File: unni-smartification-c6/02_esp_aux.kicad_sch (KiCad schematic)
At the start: 61 parts, among them J11 Conn_01x01, J12 Conn_01x01, J13 Conn_01x01, J14 Conn_01x01, J15 Conn_01x01, J17 Conn_01x01, J18 Conn_01x01, J19 Conn_01x01, J2 Li-Ion 1S JST-PH, J23 Conn_01x01, J24 Conn_01x01, J25 Conn_01x01, J26 Conn_01x01, J27 Conn_01x01, Q1 AO3401A, Q10 AO3400A touch emulator, SW1 RESET, SW2 BOOT, U1 MCP73831T-2ACI/OT, U10 ESP32-C6-MINI-1, U2 TPS63031DSK

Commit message: Clean up power nets and routing rules
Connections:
- net CONN_USB_N renamed USB_RAW_N
- net CONN_USB_P renamed USB_RAW_P
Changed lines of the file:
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@@
 	)
 	(junction
-		(at 43.18 132.715)
+		(at 43.18 132.08)
 		(diameter 0)
 		(color 0 0 0 0)
@@
 	(wire
 		(pts
-			(xy 43.18 132.715) (xy 43.18 139.7)
+			(xy 43.18 132.08) (xy 43.18 139.7)
 		)
 		(stroke
@@
 	(wire
 		(pts
-			(xy 43.18 129.54) (xy 43.18 132.715)
+			(xy 43.18 129.54) (xy 43.18 132.08)
 		)
 		(stroke
@@
 		)
 	)
-	(global_label "CONN_GND"
+	(global_label "GND"
 		(shape input)
 		(at 82.55 226.06 180)
@@
 		)
 	)
-	(global_label "CONN_VBUS"
+	(global_label "VBUS"
 		(shape input)
 		(at 77.47 243.84 270)
@@
 		)
 	)
-	(global_label "CONN_USB_P"
+	(global_label "USB_RAW_P"
 		(shape bidirectional)
 		(at 365.76 60.96 0)
@@
 		)
 	)
-	(global_label "CONN_GND"
+	(global_label "GND"
 		(shape input)
 		(at 195.58 238.76 180)
@@
 		)
 	)
-	(global_label "CONN_+BATT"
+	(global_label "+BATT"
 		(shape input)
 		(at 87.63 243.84 270)
@@
 		)
 	)
-	(global_label "CONN_VBUS"
+	(global_label "VBUS"
 		(shape input)
 		(at 43.18 217.17 180)
@@
 		)
 	)
-	(global_label "CONN_GND"
+	(global_label "GND"
 		(shape input)
 		(at 195.58 210.82 180)
@@
 		)
 	)
-	(global_label "CONN_GND"
+	(global_label "GND"
 		(shape input)
 		(at 43.18 201.93 180)
@@
 		)
 	)
-	(global_label "CONN_USB_N"
+	(global_label "USB_RAW_N"
 		(shape bidirectional)
 		(at 43.18 205.74 180)
@@
 		)
 	)
-	(global_label "CONN_USB_P"
+	(global_label "USB_RAW_P"
 		(shape bidirectional)
 		(at 43.18 209.55 180)
@@
 		)
 	)
-	(global_label "CONN_+BATT"
+	(global_label "+BATT"
 		(shape input)
 		(at 43.18 220.98 180)
@@
 		)
 	)
-	(global_label "CONN_GND"
+	(global_label "GND"
 		(shape input)
 		(at 284.48 177.8 180)
@@
 		)
 	)
-	(global_label "CONN_USB_N"
+	(global_label "USB_RAW_N"
 		(shape bidirectional)
 		(at 386.08 58.42 0)
@@
 		(unit 1)
 		(body_style 1)
-		(exclude_from_sim no)
+		(exclude_from_sim yes)
 		(in_bom yes)
 		(on_board yes)
@@
 		(unit 1)
 		(body_style 1)
-		(exclude_from_sim no)
+		(exclude_from_sim yes)
 		(in_bom yes)
 		(on_board yes)
@@
 		(unit 1)
 		(body_style 1)
-		(exclude_from_sim no)
+		(exclude_from_sim yes)
 		(in_bom yes)
 		(on_board yes)
@@
 		(unit 1)
 		(body_style 1)
-		(exclude_from_sim no)
+		(exclude_from_sim yes)
 		(in_bom yes)
 		(on_board yes)
@@
 		(unit 1)
 		(body_style 1)
-		(exclude_from_sim no)
+		(exclude_from_sim yes)
 		(in_bom yes)
 		(on_board yes)
@@
 		(unit 1)
 		(body_style 1)
-		(exclude_from_sim no)
+		(exclude_from_sim yes)
 		(in_bom yes)
 		(on_board yes)
@@
 		(unit 1)
 		(body_style 1)
-		(exclude_from_sim no)
+		(exclude_from_sim yes)
 		(in_bom yes)
 		(on_board yes)
@@
 		(unit 1)
 		(body_style 1)
-		(exclude_from_sim no)
+		(exclude_from_sim yes)
 		(in_bom yes)
 		(on_board yes)
@@
 		(unit 1)
 		(body_style 1)
-		(exclude_from_sim no)
+		(exclude_from_sim yes)
 		(in_bom yes)
 		(on_board yes)
@@
 		(unit 1)
 		(body_style 1)
-		(exclude_from_sim no)
+		(exclude_from_sim yes)
 		(in_bom yes)
 		(on_board yes)
@@
 		(unit 1)
 		(body_style 1)
-		(exclude_from_sim no)
+		(exclude_from_sim yes)
 		(in_bom yes)
 		(on_board yes)
@@
 		(unit 1)
 		(body_style 1)
-		(exclude_from_sim no)
+		(exclude_from_sim yes)
 		(in_bom yes)
 		(on_board yes)
@@
 	(symbol
 		(lib_id "power:PWR_FLAG")
-		(at 43.18 132.715 270)
+		(at 43.18 132.08 270)
 		(unit 1)
 		(body_style 1)
@@
 		(fields_autoplaced yes)
 		(property "Reference" "#FLG05"
-			(at 45.085 132.715 0)
+			(at 45.085 132.08 0)
 			(hide yes)
 			(show_name no)
@@
 		)
 		(property "Footprint" ""
-			(at 43.18 132.715 0)
+			(at 43.18 132.08 0)
 			(hide yes)
 			(show_name no)
@@
 		)
 		(property "Datasheet" ""
-			(at 43.18 132.715 0)
+			(at 43.18 132.08 0)
 			(hide yes)
 			(show_name no)
@@
 		)
 		(property "Description" "Special symbol for telling ERC where power comes from"
-			(at 43.18 132.715 0)
+			(at 43.18 132.08 0)
 			(hide yes)
 			(show_name no)
@@
 		(unit 1)
 		(body_style 1)
-		(exclude_from_sim no)
+		(exclude_from_sim yes)
 		(in_bom yes)
 		(on_board yes)
@@
 		(unit 1)
 		(body_style 1)
-		(exclude_from_sim no)
+		(exclude_from_sim yes)
 		(in_bom yes)
 		(on_board yes)

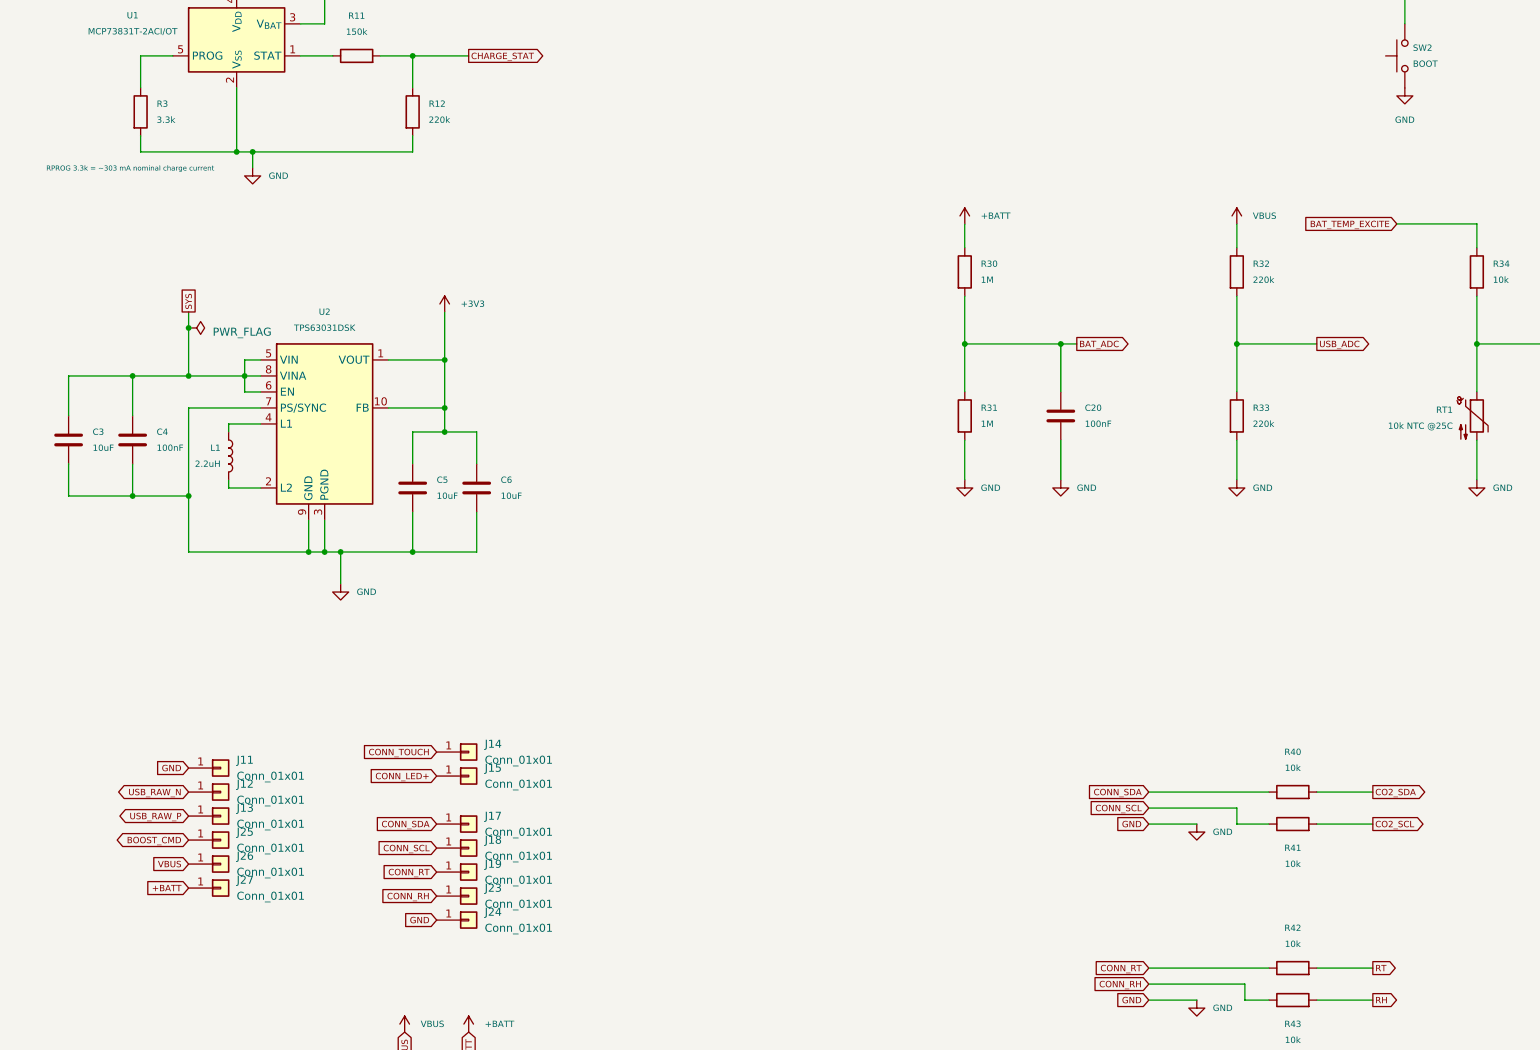
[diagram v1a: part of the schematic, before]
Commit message: new tvs diode, final fiddlings
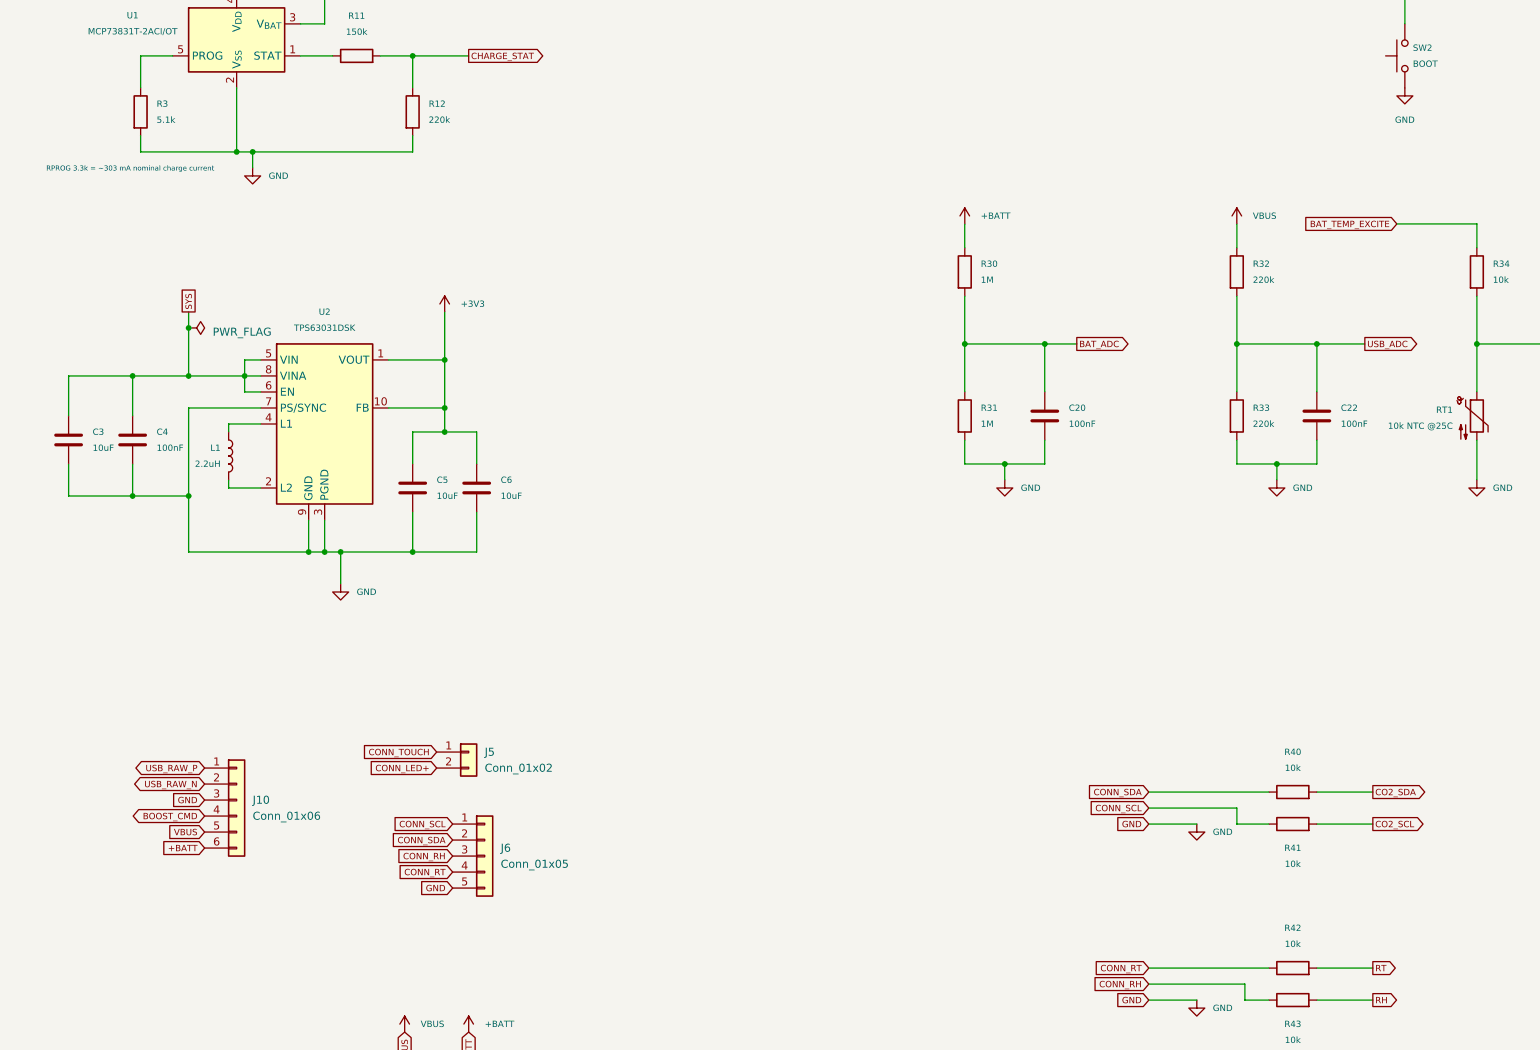
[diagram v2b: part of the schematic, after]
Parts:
- removed J11, J24: Conn_01x01, Connector_Wire:SolderWire-0.5sqmm_1x01_D0.9mm_OD2.1mm, symbol Connector_Generic:Conn_01x01
- removed J12, J13, J14, J15, J17, J18, J19, J23, J25, J26, J27: Conn_01x01, Connector_Wire:SolderWire-0.1sqmm_1x01_D0.4mm_OD1mm, symbol Connector_Generic:Conn_01x01
- added C22: 100nF, Capacitor_SMD:C_0603_1608Metric_Pad1.08x0.95mm_HandSolder, symbol Device:C
- added J10: Conn_01x06, Connector_JST:JST_PH_B6B-PH-K_1x06_P2.00mm_Vertical, symbol Connector_Generic:Conn_01x06
- added J5: Conn_01x02, Connector_JST:JST_PH_B2B-PH-K_1x02_P2.00mm_Vertical, symbol Connector_Generic:Conn_01x02
- added J6: Conn_01x05, Connector_JST:JST_PH_B5B-PH-K_1x05_P2.00mm_Vertical, symbol Connector_Generic:Conn_01x05
- J2: footprint Connector_JST:JST_PH_S2B-PH-K_1x02_P2.00mm_Horizontal -> Connector_JST:JST_PH_B2B-PH-K_1x02_P2.00mm_Vertical
- R3: value 3.3k -> 5.1k
- R40, R41, R42, R43: footprint Resistor_SMD:R_0805_2012Metric_Pad1.20x1.40mm_HandSolder -> Resistor_SMD:R_0603_1608Metric_Pad0.98x0.95mm_HandSolder
- RT1: footprint Connector_PinSocket_2.54mm:PinSocket_1x02_P2.54mm_Vertical -> Connector_JST:JST_PH_B2B-PH-K_1x02_P2.00mm_Vertical
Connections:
- net +BATT: now also J10.6 (Pin_6)
- net BOOST_CMD: now also J10.4 (Pin_4)
- net CONN_LED+: now also J5.2 (Pin_2)
- net CONN_RH: now also J6.3 (Pin_3)
- net CONN_RT: now also J6.4 (Pin_4)
- net CONN_SCL: now also J6.1 (Pin_1)
- net CONN_SDA: now also J6.2 (Pin_2)
- net CONN_TOUCH: now also J5.1 (Pin_1)
- net GND: now also C22.2, J10.3 (Pin_3), J6.5 (Pin_5)
- net USB_ADC: now also C22.1
- net USB_RAW_N: now also J10.2 (Pin_2)
- net USB_RAW_P: now also J10.1 (Pin_1)
- net VBUS: now also J10.5 (Pin_5)
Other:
- moved on the sheet: C20

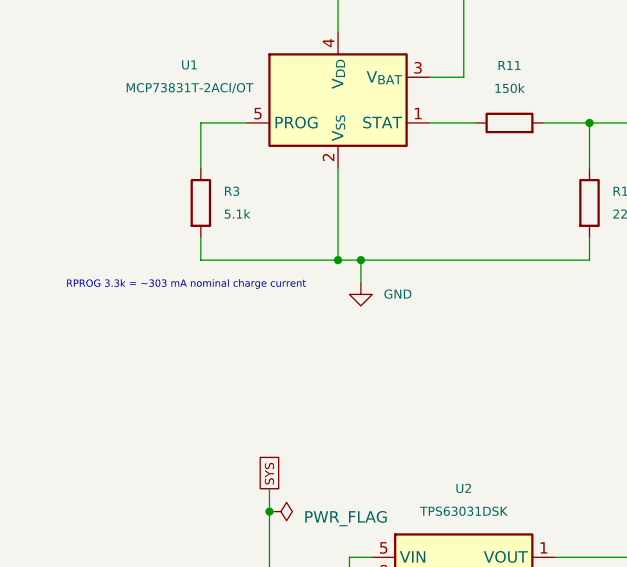
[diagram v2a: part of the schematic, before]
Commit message: Align stackup and validation with JLCPCB
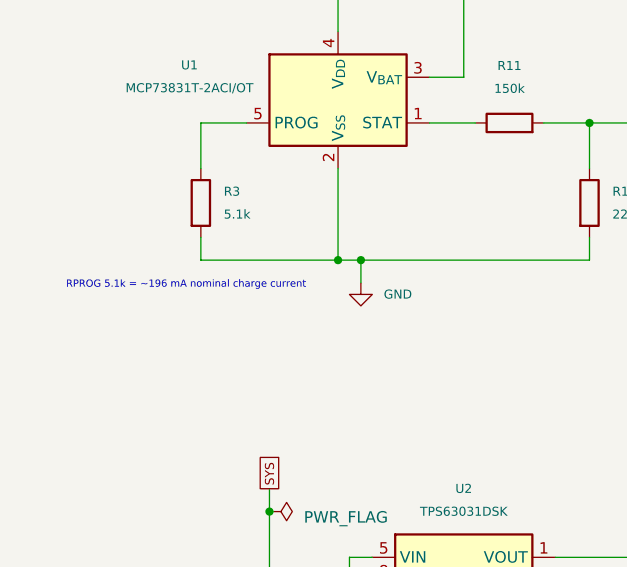
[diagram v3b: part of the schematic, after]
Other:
- note added: "RPROG 5.1k = ~196 mA nominal charge current"
- note removed: "RPROG 3.3k = ~303 mA nominal charge current"
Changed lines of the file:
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@@
 		)
 	)
-	(text "RPROG 3.3k = ~303 mA nominal charge current"
+	(text "RPROG 5.1k = ~196 mA nominal charge current"
 		(exclude_from_sim no)
 		(at 20.574 107.442 0)

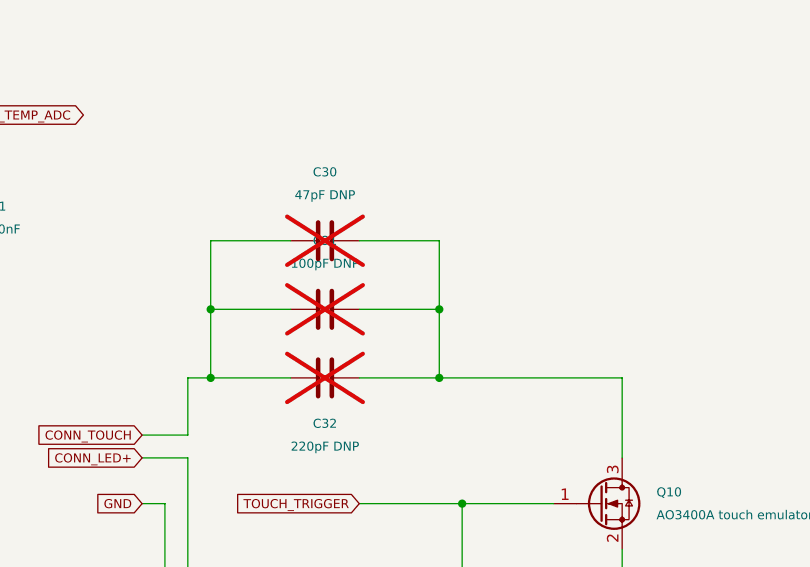
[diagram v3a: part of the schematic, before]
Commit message: cleanups, silkscreen
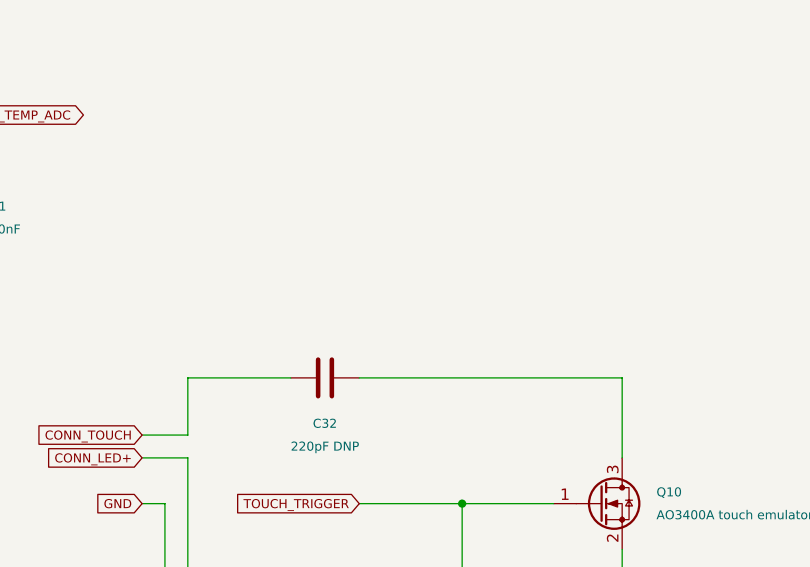
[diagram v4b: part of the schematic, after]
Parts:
- removed C30: 47pF DNP, Capacitor_SMD:C_0603_1608Metric_Pad1.08x0.95mm_HandSolder, symbol Device:C
- removed C31: 100pF DNP, Capacitor_SMD:C_0603_1608Metric_Pad1.08x0.95mm_HandSolder, symbol Device:C
- C32: now fitted

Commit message: silkscreen beautification
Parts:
- J5, J6: now not fitted
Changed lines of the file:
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@@
 		(on_board yes)
 		(in_pos_files yes)
-		(dnp no)
+		(dnp yes)
 		(fields_autoplaced yes)
 		(property "Reference" "J6"
@@
 		(on_board yes)
 		(in_pos_files yes)
-		(dnp no)
+		(dnp yes)
 		(fields_autoplaced yes)
 		(property "Reference" "J5"

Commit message: redid some routing, add btn for manual measurements from unni
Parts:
- J5: footprint Connector_JST:JST_PH_B2B-PH-K_1x02_P2.00mm_Vertical -> Connector_JST:JST_PH_B3B-PH-K_1x03_P2.00mm_Vertical; symbol Connector_Generic:Conn_01x02 -> Connector_Generic:Conn_01x03
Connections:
- net CONN_BTN: now reaches U10.28 (IO22)
- net CONN_BTN: now also J5.3 (Pin_3)
- no-connect marks 7 -> 5
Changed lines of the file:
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@@
 	)
 	(no_connect
-		(at 267.97 76.2)
-	)
-	(no_connect
 		(at 267.97 68.58)
 	)
 	(no_connect
-		(at 267.97 66.04)
-	)
-	(no_connect
-		(at 311.15 81.28)
+		(at 298.45 66.04)
 	)
 	(no_connect
-		(at 298.45 66.04)
+		(at 267.97 66.04)
 	)
 	(no_connect
@@
 		)
 	)
+	(global_label "CONN_LED+"
+		(shape input)
+		(at 82.55 199.39 180)
+		(fields_autoplaced yes)
+		(effects
+			(font
+				(size 1 1)
+			)
+			(justify right)
+		)
+		(property "Intersheetrefs" "${INTERSHEET_REFS}"
+			(at 71.3426 199.39 0)
+			(hide yes)
+			(show_name no)
+			(do_not_autoplace no)
+			(effects
+				(font
+					(size 1.27 1.27)
+				)
+				(justify right)
+			)
+		)
+	)
 	(global_label "GND"
 		(shape input)
@@
 		)
 	)
-	(global_label "CONN_LED+"
+	(global_label "CONN_TOUCH"
 		(shape input)
-		(at 82.55 201.93 180)
+		(at 82.55 196.85 180)
 		(fields_autoplaced yes)
 		(effects
@@
 		)
 		(property "Intersheetrefs" "${INTERSHEET_REFS}"
-			(at 71.3426 201.93 0)
+			(at 70.3903 196.85 0)
 			(hide yes)
 			(show_name no)
@@
 		)
 	)
+	(global_label "CONN_BTN"
+		(shape input)
+		(at 82.55 201.93 180)
+		(fields_autoplaced yes)
+		(effects
+			(font
+				(size 1 1)
+			)
+			(justify right)
+		)
+		(property "Intersheetrefs" "${INTERSHEET_REFS}"
+			(at 72.4855 201.93 0)
+			(hide yes)
+			(show_name no)
+			(do_not_autoplace no)
+			(effects
+				(font
+					(size 1.27 1.27)
+				)
+				(justify right)
+			)
+		)
+	)
+	(global_label "CONN_BTN"
+		(shape input)
+		(at 311.15 81.28 0)
+		(fields_autoplaced yes)
+		(effects
+			(font
+				(size 1 1)
+			)
+			(justify left)
+		)
+		(property "Intersheetrefs" "${INTERSHEET_REFS}"
+			(at 321.2145 81.28 0)
+			(hide yes)
+			(show_name no)
+			(do_not_autoplace no)
+			(effects
+				(font
+					(size 1.27 1.27)
+				)
+				(justify left)
+			)
+		)
+	)
 	(global_label "CONN_RH"
 		(shape input)
@@
 		)
 	)
-	(global_label "CONN_TOUCH"
-		(shape input)
-		(at 82.55 199.39 180)
-		(fields_autoplaced yes)
-		(effects
-			(font
-				(size 1 1)
-			)
-			(justify right)
-		)
-		(property "Intersheetrefs" "${INTERSHEET_REFS}"
-			(at 70.3903 199.39 0)
-			(hide yes)
-			(show_name no)
-			(do_not_autoplace no)
-			(effects
-				(font
-					(size 1.27 1.27)
-				)
-				(justify right)
-			)
-		)
-	)
 	(global_label "BAT_TEMP_EXCITE"
 		(shape output)
@@
 	)
 	(symbol
-		(lib_id "Connector_Generic:Conn_01x02")
+		(lib_id "Connector_Generic:Conn_01x03")
 		(at 87.63 199.39 0)
 		(unit 1)
 		(body_style 1)
-		(exclude_from_sim yes)
+		(exclude_from_sim no)
 		(in_bom yes)
 		(on_board yes)
@@
 		(fields_autoplaced yes)
 		(property "Reference" "J5"
-			(at 90.17 199.3899 0)
+			(at 90.17 198.1199 0)
 			(show_name no)
 			(do_not_autoplace no)
@@
 		)
 		(property "Value" "Conn_01x02"
-			(at 90.17 201.9299 0)
+			(at 90.17 200.6599 0)
 			(show_name no)
 			(do_not_autoplace no)
@@
 			)
 		)
-		(property "Footprint" "Connector_JST:JST_PH_B2B-PH-K_1x02_P2.00mm_Vertical"
+		(property "Footprint" "Connector_JST:JST_PH_B3B-PH-K_1x03_P2.00mm_Vertical"
 			(at 87.63 199.39 0)
 			(hide yes)
@@
 			)
 		)
-		(property "Description" "Generic connector, single row, 01x02, script generated (kicad-library-utils/schlib/autogen/connector/)"
+		(property "Description" "Generic connector, single row, 01x03, script generated (kicad-library-utils/schlib/autogen/connector/)"
 			(at 87.63 199.39 0)
 			(hide yes)
@@
 		(pin "1"
 		)
+		(pin "3"
+		)
 		(instances
